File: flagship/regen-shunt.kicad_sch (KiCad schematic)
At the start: 15 parts, among them J3 EXT_SHUNT, Q6 CLAMP_FET_100V, U3 TLV1805, U4 TLV431

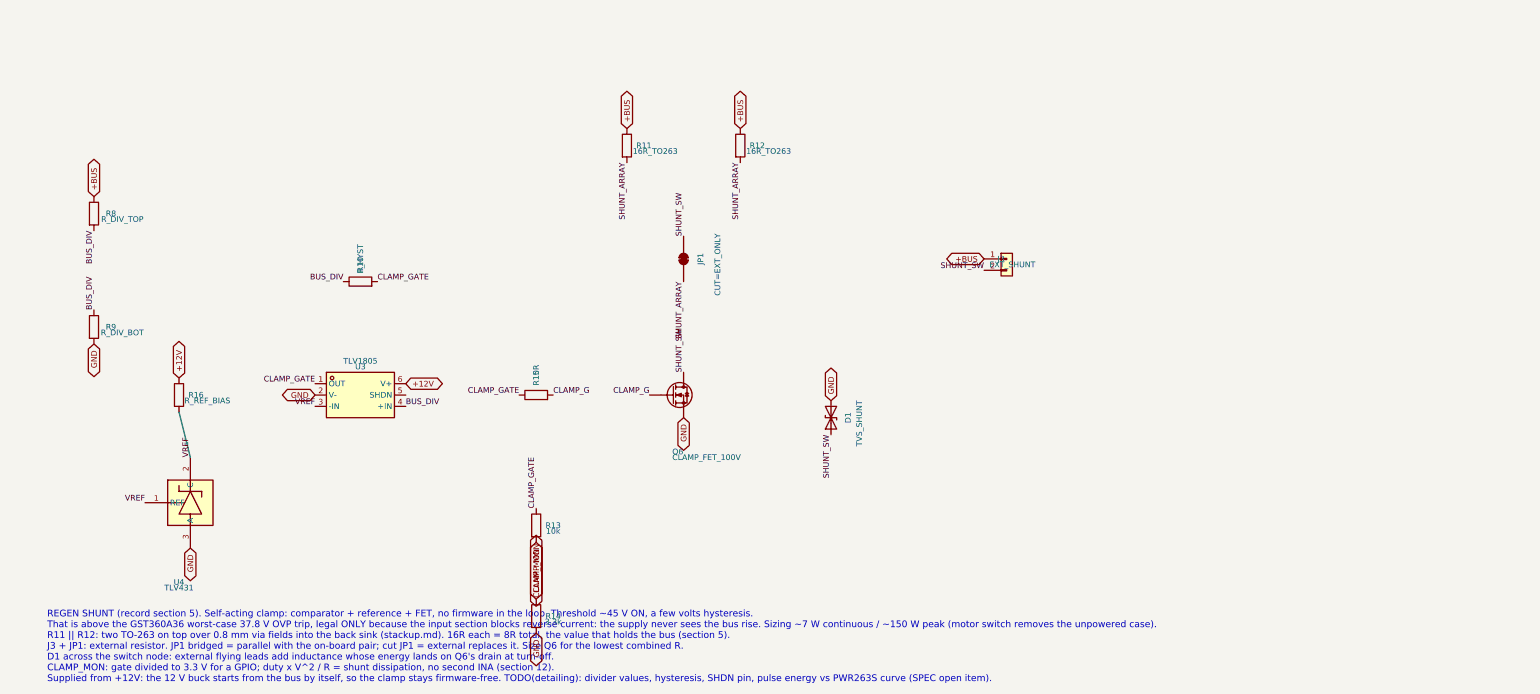
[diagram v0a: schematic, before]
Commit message: flagship: regen shunt detailed and drawn as a wired circuit
Power section (R509 || R510 -> JP501 -> Q501, J3 + D501 on the switch node) beside the
self-acting comparator clamp (TLV1805 + TLV431): ON 44.7 V / OFF 41.7 V, 1 nF filter,
47 R gate drive; the CLAMP_MON divider doubles as the gate pull-down. Verified: all 10
sheet nets match the intended table exactly; ERC 0 errors after typing the comparator
and reference pins.

Co-Authored-By: Claude Opus 5.5 (1M context) <noreply@anthropic.com>
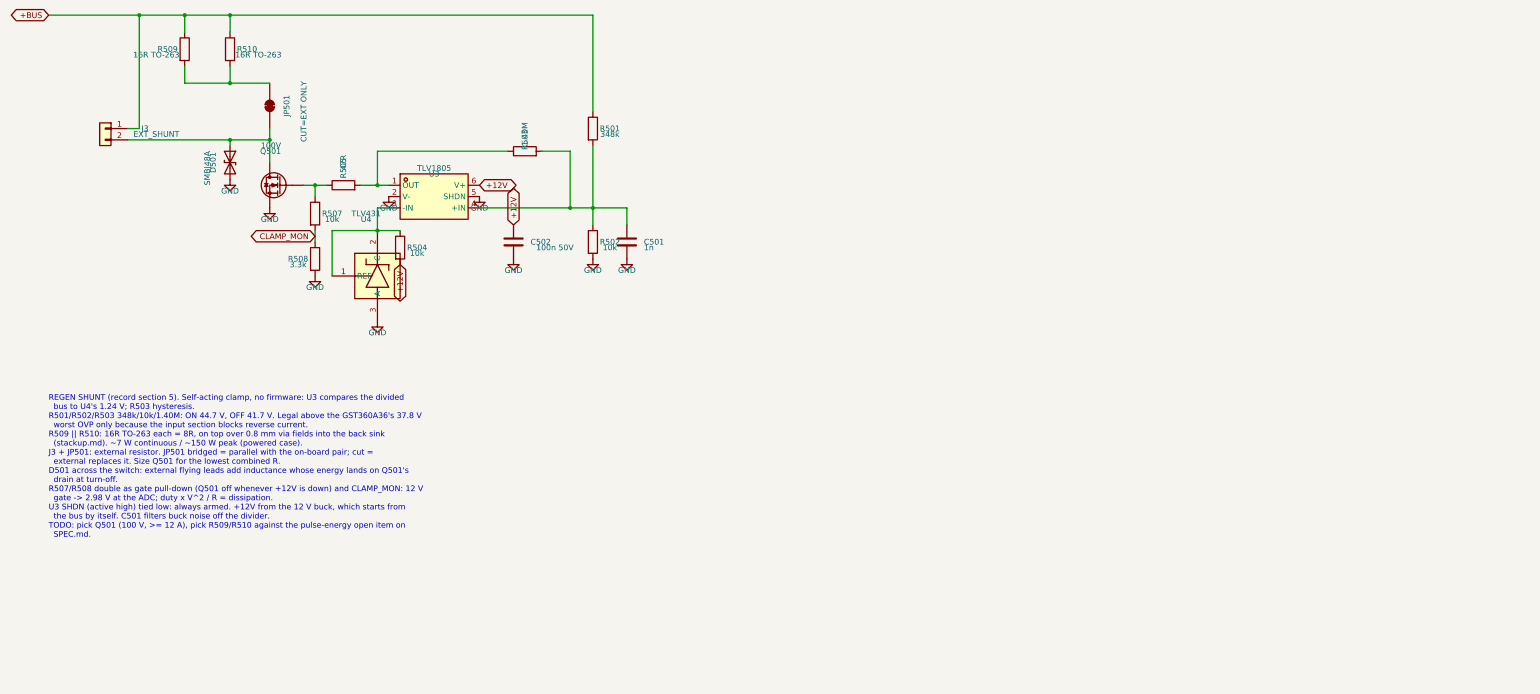
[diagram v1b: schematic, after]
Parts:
- removed D1: TVS_SHUNT, symbol Device:D_TVS
- removed JP1: CUT=EXT_ONLY, symbol Jumper:SolderJumper_2_Bridged
- removed Q6: CLAMP_FET_100V, symbol Device:Q_NMOS
- removed R10: R_HYST, Resistor_SMD:R_0805_2012Metric, symbol Device:R
- removed R11, R12: 16R_TO263, symbol Device:R
- removed R13: 10k, Resistor_SMD:R_0805_2012Metric, symbol Device:R
- removed R14: 3.3k, Resistor_SMD:R_0805_2012Metric, symbol Device:R
- removed R15: 10R, Resistor_SMD:R_0805_2012Metric, symbol Device:R
- removed R16: R_REF_BIAS, Resistor_SMD:R_0805_2012Metric, symbol Device:R
- removed R8: R_DIV_TOP, Resistor_SMD:R_1206_3216Metric, symbol Device:R
- removed R9: R_DIV_BOT, Resistor_SMD:R_0805_2012Metric, symbol Device:R
- added C501: 1n, Capacitor_SMD:C_0805_2012Metric, symbol Device:C
- added C502: 100n 50V, Capacitor_SMD:C_0805_2012Metric, symbol Device:C
- added D501: SMBJ48A, Diode_SMD:D_SMB, symbol Device:D_TVS
- added JP501: CUT=EXT ONLY, symbol Jumper:SolderJumper_2_Bridged
- added Q501: 100V, symbol Device:Q_NMOS
- added R501: 348k, Resistor_SMD:R_1206_3216Metric, symbol Device:R
- added R502, R504, R507: 10k, Resistor_SMD:R_0805_2012Metric, symbol Device:R
- added R503: 1.40M, Resistor_SMD:R_0805_2012Metric, symbol Device:R
- added R505: 47R, Resistor_SMD:R_0805_2012Metric, symbol Device:R
- added R508: 3.3k, Resistor_SMD:R_0805_2012Metric, symbol Device:R
- added R509, R510: 16R TO-263, flagship:TO-263-2_L10.1-W8.8-P5.08-LS15.4-TL, symbol Device:R
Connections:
- net +12V: now also C502.1, R504.2
- net +BUS: now also R501.1, R509.1, R510.1
- net CLAMP_MON: now also R507.2, R508.1
- net GND: now also U3.5 (SHDN), C501.2, C502.2, D501.2 (A2), Q501.S, R502.2, R508.2
- net BUS_DIV: no longer names the net of U3.4 (+IN)
- net BUS_DIV: now also C501.1, R501.2, R502.1, R503.2
- net CLAMP_GATE: no longer names the net of U3.1 (OUT)
- net CLAMP_GATE: now also R503.1, R505.2
- net SHUNT_SW: no longer names the net of J3.2 (Pin_2)
- net SHUNT_SW: now also D501.1 (A1), JP501.1 (A), Q501.D
- net VREF: no longer names the net of U3.3 (-IN), U4.1 (REF), U4.2 (C)
- net VREF: now also R504.1
- new net: Q501.G, R505.1, R507.1
- new net: JP501.2 (B), R509.2, R510.2
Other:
- note added: "REGEN SHUNT (record section 5). Self-acting clamp, no firmware: U3 compares the divided bus to U4's 1.24 V; R503 hysteresis. R501/R502/R503 348k/10k/1.40M: ON 44.7 V, OFF 41.7 V. Legal above the GST360A36's 37.8 V worst OVP only because the input section blocks reverse current. R509 || R510: 16R TO-263 each = 8R, on top over 0.8 mm via fields into the back sink (stackup.md). ~7 W continuous / ~15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"
- note removed: "REGEN SHUNT (record section 5). Self-acting clamp: comparator + reference + FET, no firmware in the loop. Threshold ~45 V ON, a few volts hysteresis. That is above the GST360A36 worst-case 37.8 V OVP trip, legal ONLY because the input section blocks reverse current: the supply never sees the bus rise. Sizing ~7 W continuous / ~150 W peak (motor switch removes the unpowered case). R11 || R12: two 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"
